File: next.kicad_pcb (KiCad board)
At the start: 2 copper layers, 351.4 x 100.4 mm, 184 parts, among them J1 USB_mini_micro_B, K0:0 KEYSW, K0:1 KEYSW, K0:10 KEYSW, K0:11 KEYSW, K0:12 KEYSW, K0:13 KEYSW, K0:14 KEYSW, K0:15 KEYSW, K0:16 KEYSW, K0:2 KEYSW, K0:3 KEYSW, K0:3_1 KEYSW, K0:4 KEYSW, K0:5 KEYSW, K0:6 KEYSW, K0:7 KEYSW, K0:8 KEYSW, K0:9 KEYSW, K1:0 KEYSW, K1:1 KEYSW, K1:10 KEYSW, K1:11 KEYSW, K1:12 KEYSW, K1:13 KEYSW, K1:14 KEYSW, K1:15 KEYSW, K1:16 KEYSW, K1:2 KEYSW, K1:3 KEYSW, K1:4 KEYSW, K1:5 KEYSW, K1:6 KEYSW, K1:7 KEYSW, K1:8 KEYSW, K1:9 KEYSW, K2:0 KEYSW, K2:1 KEYSW, K2:10 KEYSW, K2:11 KEYSW, K2:12 KEYSW, K2:13 KEYSW, K2:14 KEYSW, K2:15 KEYSW, K2:16 KEYSW, K2:2 KEYSW, K2:3 KEYSW, K2:4 KEYSW, K2:5 KEYSW, K2:6 KEYSW, K2:7 KEYSW, K2:8 KEYSW, K2:9 KEYSW, K3:0 KEYSW, K3:1 KEYSW, K3:10 KEYSW, K3:11 KEYSW, K3:12 KEYSW, K3:13 KEYSW, K3:14 KEYSW, K3:15 KEYSW, K3:16 KEYSW, K3:2 KEYSW, K3:3 KEYSW, K3:3_1 KEYSW, K3:4 KEYSW, K3:5 KEYSW, K3:6 KEYSW, K3:7 KEYSW, K3:8 KEYSW, K3:9 KEYSW, K4:0 KEYSW, K4:0_1 KEYSW, K4:1 KEYSW, K4:14 KEYSW, K4:15 KEYSW, K4:16 KEYSW, K4:1_1 KEYSW, K4:2 KEYSW, K4:2_1 KEYSW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

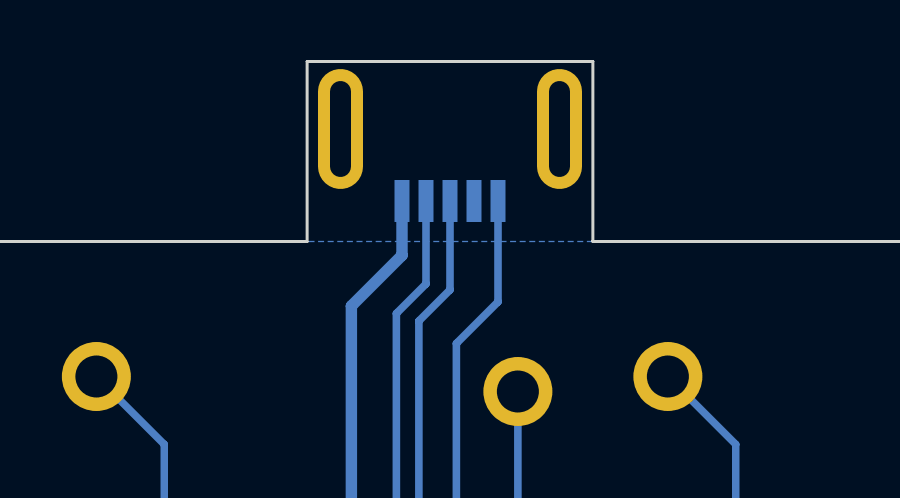
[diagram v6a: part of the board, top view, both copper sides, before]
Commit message: Adjust USB port
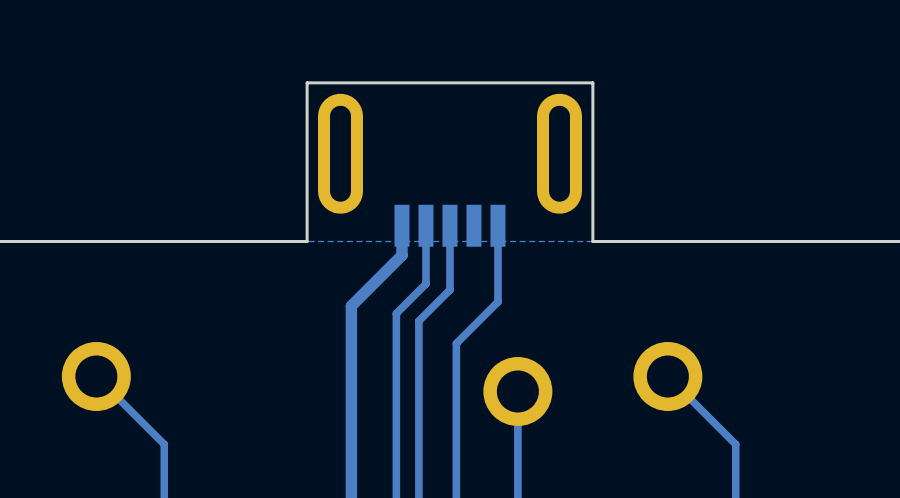
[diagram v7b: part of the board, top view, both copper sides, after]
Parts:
- moved J1 0.82 mm to (204.8, 28.6)
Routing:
- net GND: track 487.4 -> 486.6 mm
- net Net-(J1-Pad2): track 91.7 -> 90.8 mm
- net Net-(J1-Pad3): track 91.7 -> 90.8 mm
- net +5V: track 358.9 -> 358.0 mm
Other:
- board size 351.4 x 100.4 mm -> 351.4 x 99.7 mm
